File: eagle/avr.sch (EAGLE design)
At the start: 22 parts, among them IC1 MEGA8-P, IC2 7805TV, Q1 16MHz

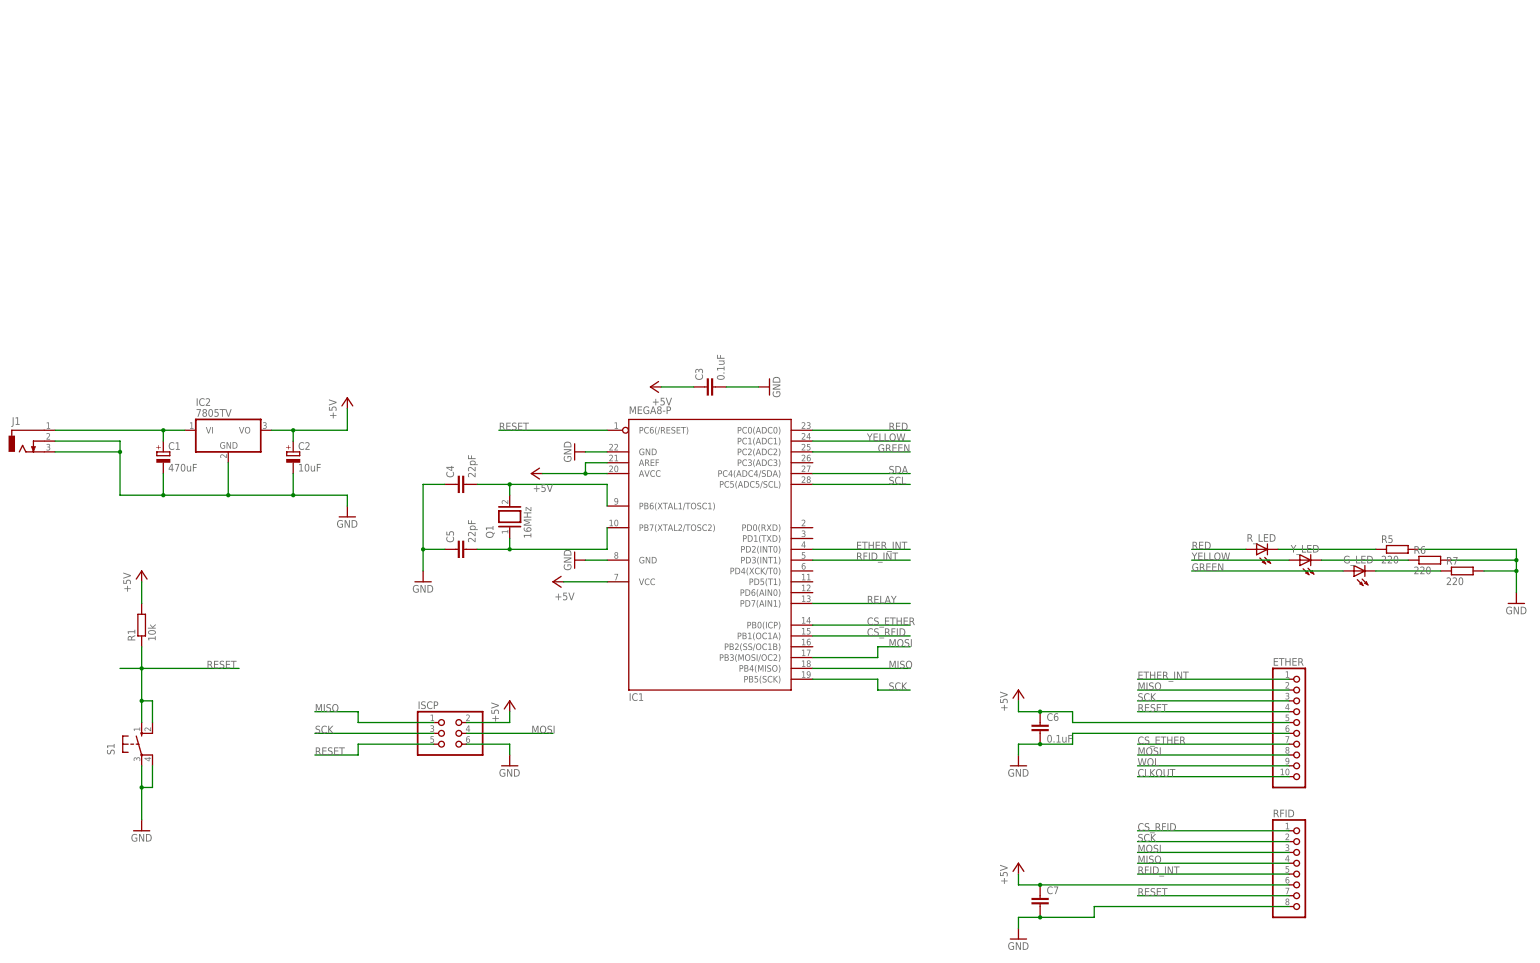
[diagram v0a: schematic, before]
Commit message: Added 3.3v supply
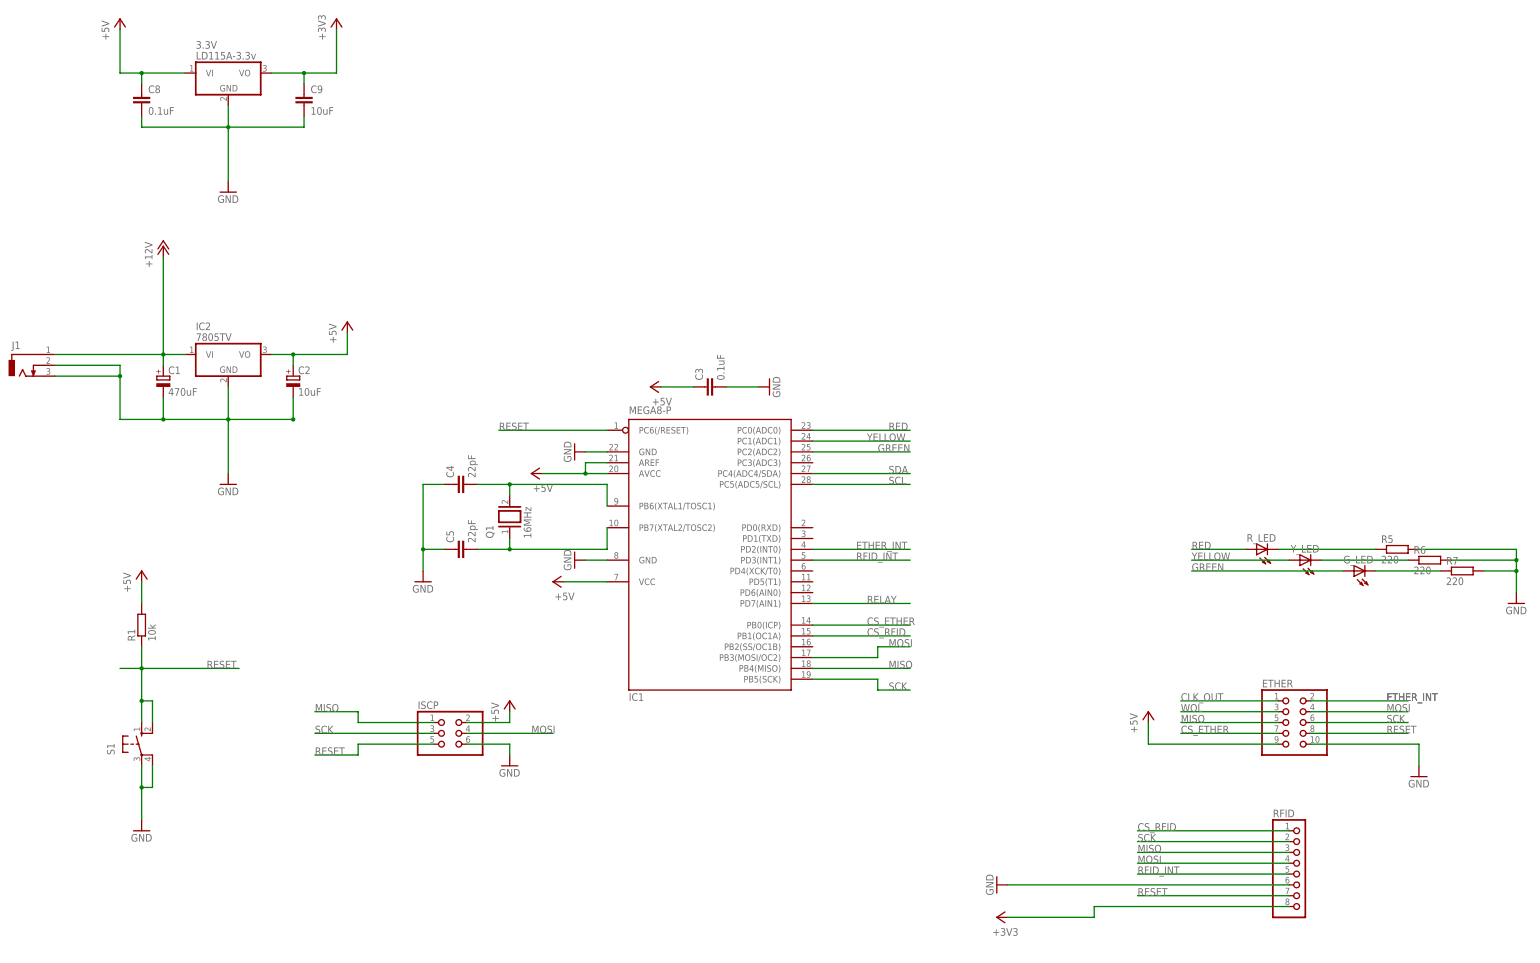
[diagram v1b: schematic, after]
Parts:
- removed C6: 0.1uF, resistor:C-EU050-025X075
- removed C7: (no value), resistor:C-EU050-025X075
- added 3.3V: LD115A-3.3v, linear:7805TV
- added C8: 0.1uF, resistor:C-EU050-025X075
- added C9: 10uF, resistor:C-EU050-025X075
- ETHER: device pinhead:PINHD-1X10 -> pinhead:PINHD-2X5
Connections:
- net N$1 renamed +12V
- removed net CLKOUT: ETHER.10
- new net +3V3: 3.3V.VO, C9.1, RFID.8
- new net CLK_OUT: ETHER.1
- net +5V: now also 3.3V.VI, C8.1, ETHER.9; no longer C6.1, C7.1, ETHER.5, RFID.6
- net ETHER_INT: now also ETHER.2; no longer ETHER.1
- net GND: now also 3.3V.GND, C8.2, C9.2, ETHER.10, RFID.6; no longer C6.2, C7.2, ETHER.6, RFID.8
- net MISO: now also ETHER.5, RFID.3; no longer ETHER.2, RFID.4
- net MOSI: now also ETHER.4, RFID.4; no longer ETHER.8, RFID.3
- net RESET: now also ETHER.8; no longer ETHER.4
- net SCK: now also ETHER.6; no longer ETHER.3
- net WOL: now also ETHER.3; no longer ETHER.9
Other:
- moved on the sheet: C1, C2, ETHER, IC2, J1

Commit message: Updated pinouts
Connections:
- net MISO: now also ETHER.4; no longer ETHER.5
- net MOSI: now also ETHER.5; no longer ETHER.4
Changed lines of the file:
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@@
 </segment>
 <segment>
-<pinref part="ETHER" gate="A" pin="5"/>
-<wire x1="274.32" y1="38.1" x2="251.46" y2="38.1" width="0.1524" layer="91"/>
-<label x="251.46" y="38.1" size="1.778" layer="95"/>
+<pinref part="ETHER" gate="A" pin="4"/>
+<wire x1="281.94" y1="40.64" x2="304.8" y2="40.64" width="0.1524" layer="91"/>
+<label x="299.72" y="40.64" size="1.778" layer="95"/>
 </segment>
 </net>
@@
 </segment>
 <segment>
-<pinref part="ETHER" gate="A" pin="4"/>
-<wire x1="281.94" y1="40.64" x2="304.8" y2="40.64" width="0.1524" layer="91"/>
-<label x="299.72" y="40.64" size="1.778" layer="95"/>
+<pinref part="ETHER" gate="A" pin="5"/>
+<wire x1="274.32" y1="38.1" x2="251.46" y2="38.1" width="0.1524" layer="91"/>
+<label x="251.46" y="38.1" size="1.778" layer="95"/>
 </segment>
 </net>
